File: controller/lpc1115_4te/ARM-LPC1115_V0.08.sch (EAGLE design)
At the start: 52 parts, among them IC2 MC34063AP, IC3 MCP1702-33, Q1 BC557B, Q3 BC640C, T1 BC547C

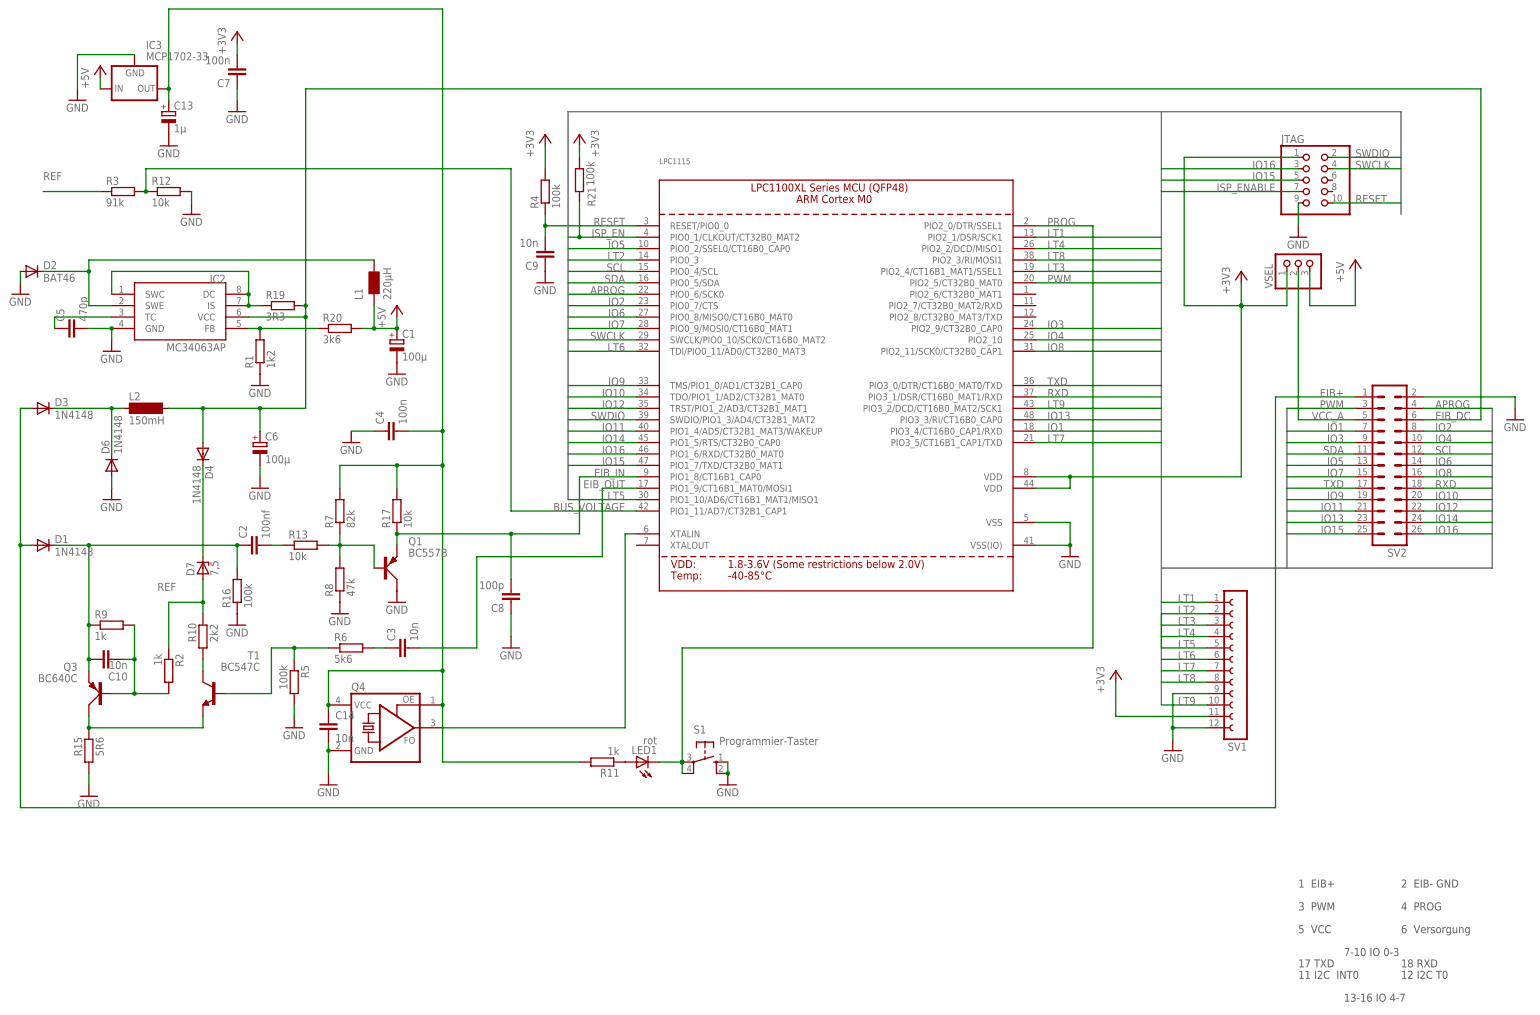
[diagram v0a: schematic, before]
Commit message: Improve layout
Changed routing to create better ground plane on bottom layer.
Add C11 to proviode better/more stable voltage supply to the CPU.
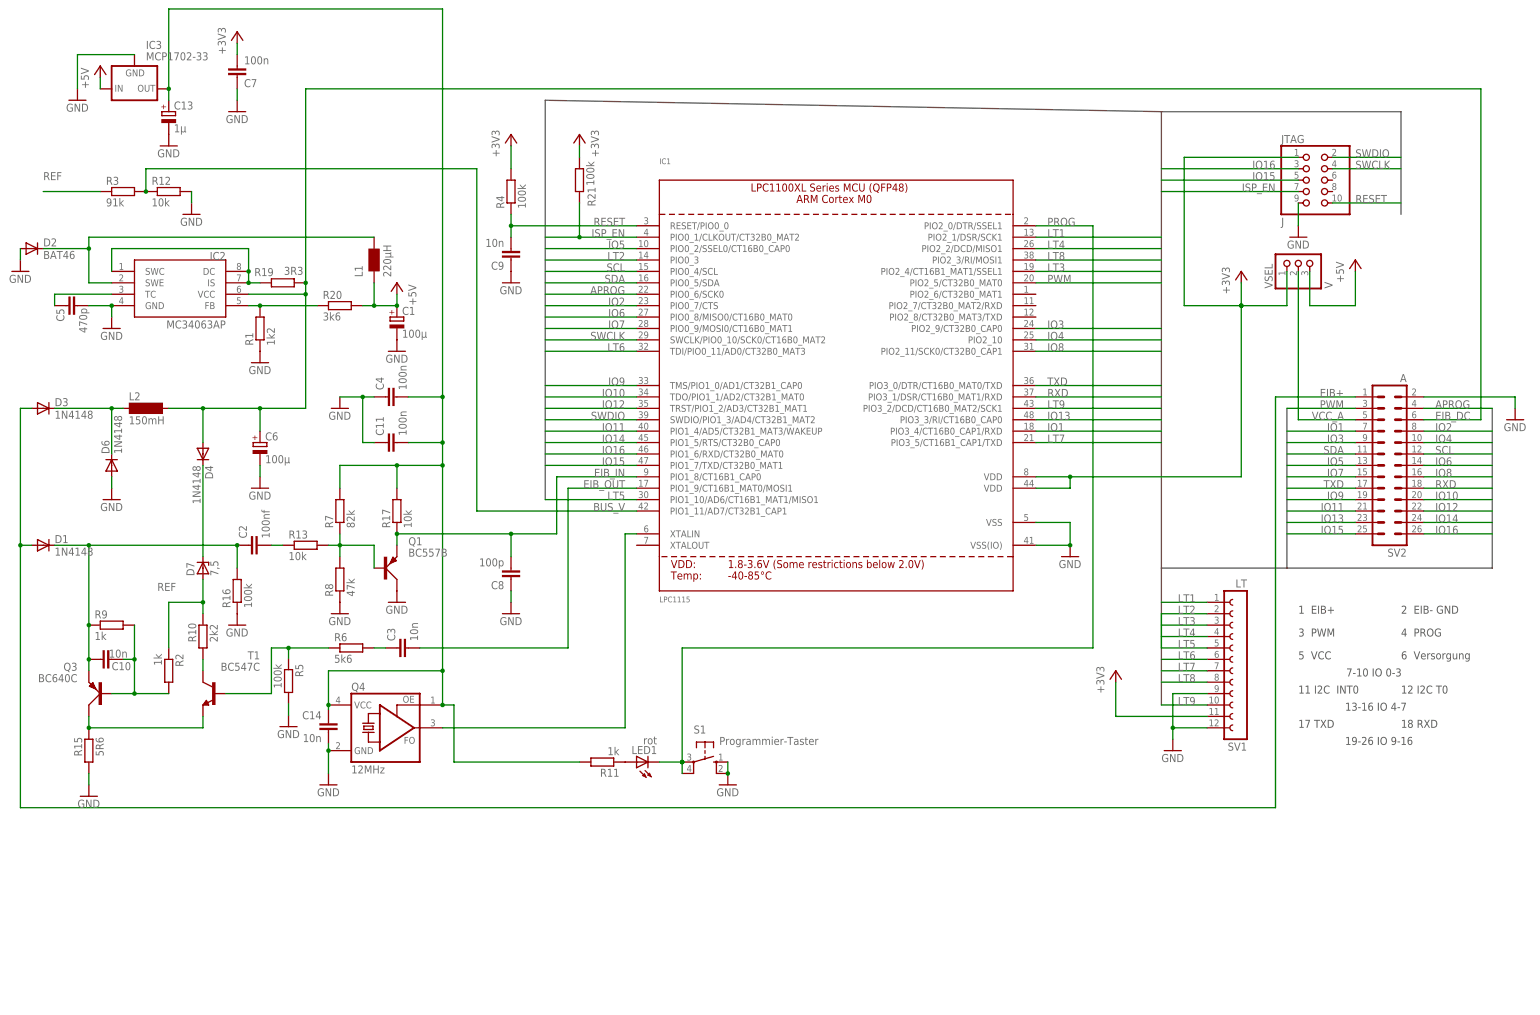
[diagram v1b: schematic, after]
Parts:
- added C11: 100n, rcl:C-EU050-024X044
- IC1: value (none) -> LPC1115
- JTAG: value (none) -> J
- Q4: value (none) -> 12MHz
- SV1: value (none) -> LT
- SV2: value (none) -> A
- VSEL: value (none) -> V
- renumbered LPC1115 to IC1
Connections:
- net BUS_VOLTAGE renamed BUS_V
- removed net ISP_ENABLE: JTAG.7
- net GND: now also C11.1
- net ISP_EN: now also JTAG.7
- net VCC_3V3: now also C11.2
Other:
- note added: "19-26 IO 9-16"
- moved on the sheet: C1, C4, C5, C8, C9, D2, IC2, L1, R1, R19, R20, R4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

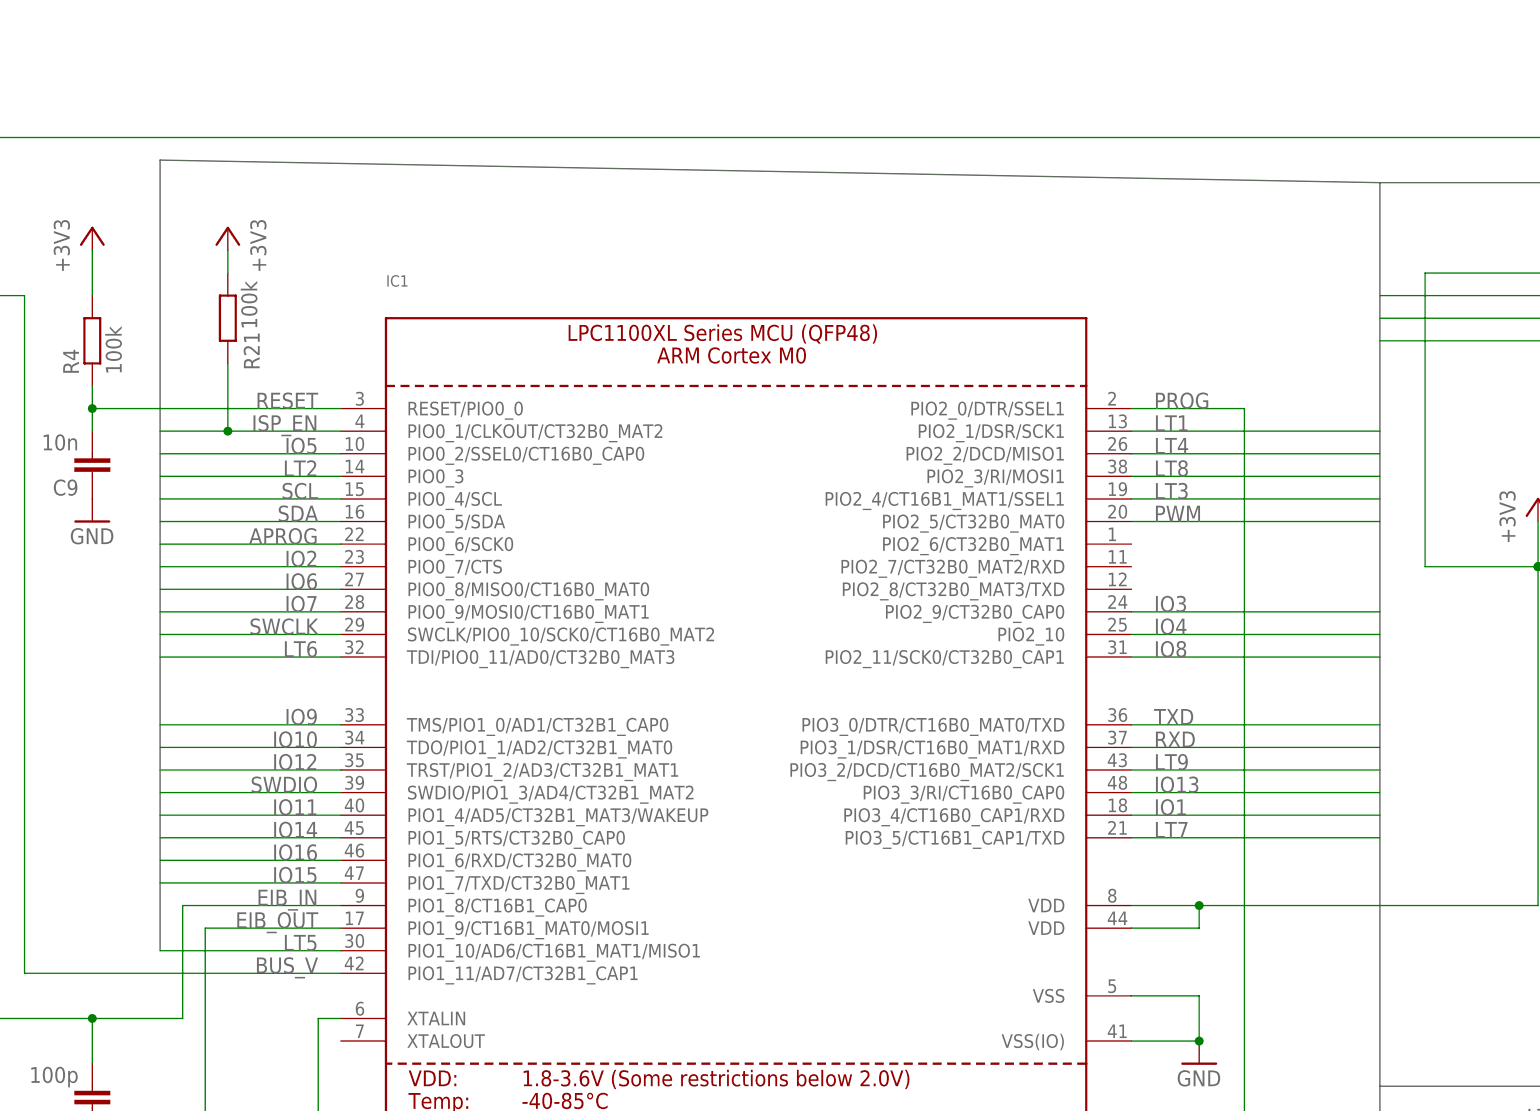
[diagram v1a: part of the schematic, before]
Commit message: Exchange PWM and LT9
To support a LPC11Uxx device and have the two pins required for the USB on
the LED/Taster pinhead the old PWM and LT9 have been swaped.
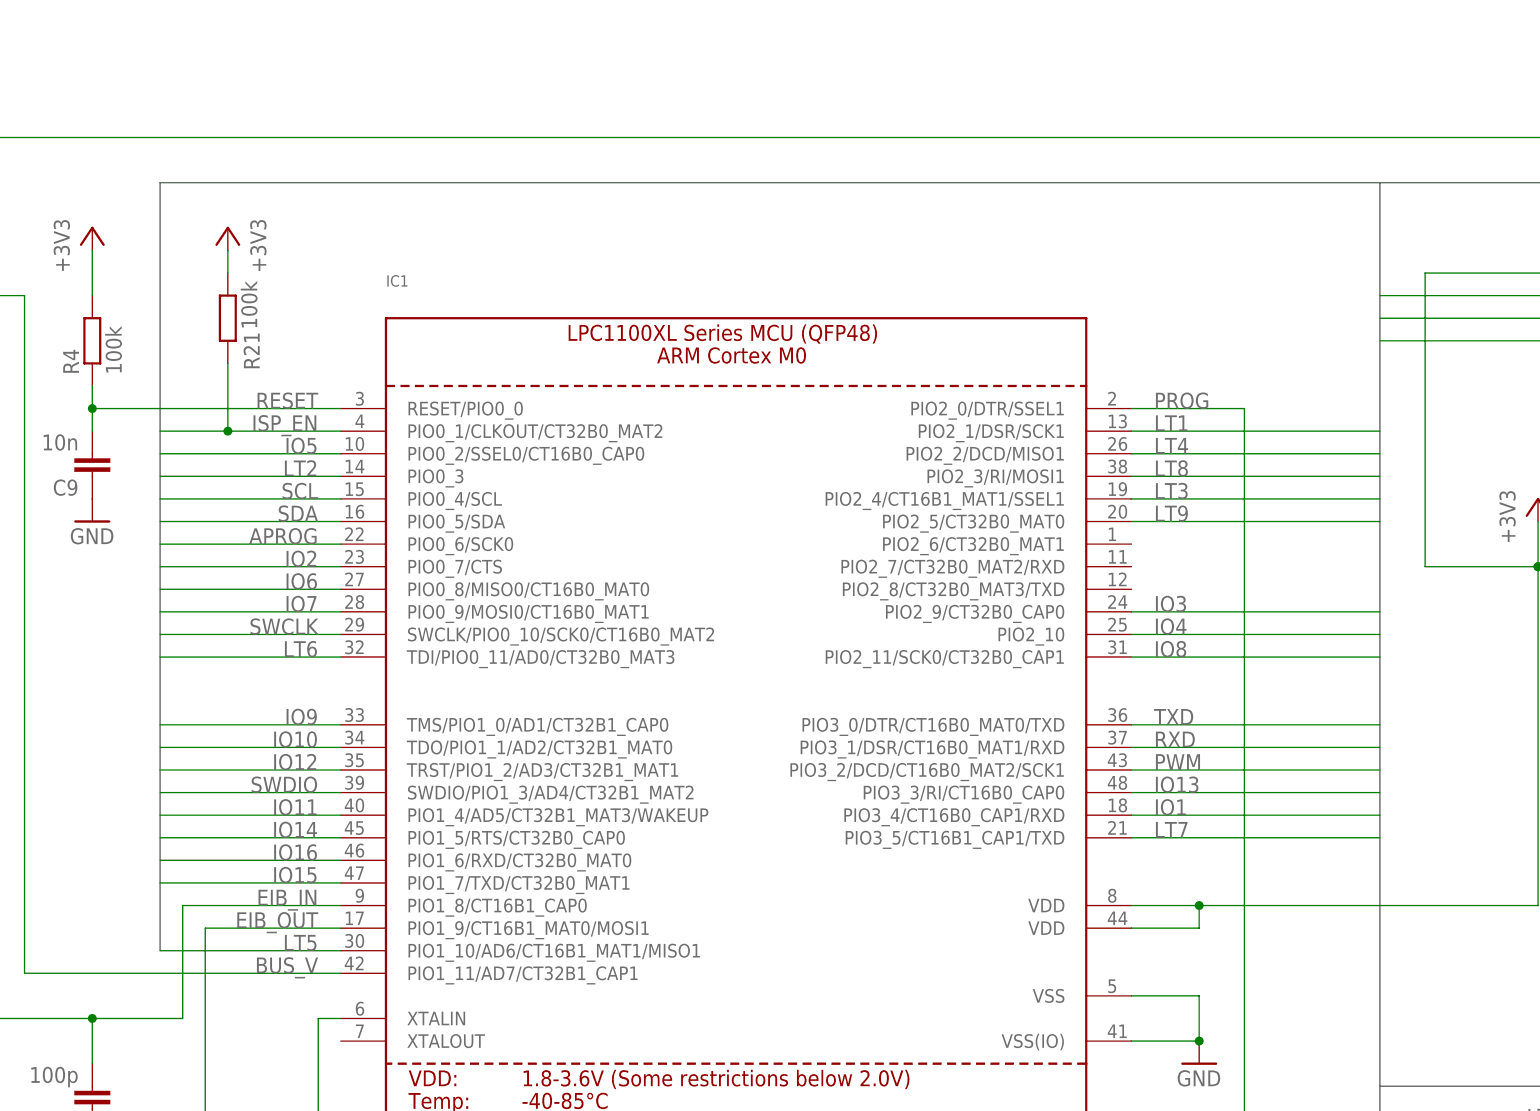
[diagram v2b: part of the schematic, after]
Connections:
- net LT9: now also IC1.PIO2_5/CT32B0_MAT0; no longer IC1.PIO3_2/DCD/CT16B0_MAT2/SCK1
- net PWM: now also IC1.PIO3_2/DCD/CT16B0_MAT2/SCK1; no longer IC1.PIO2_5/CT32B0_MAT0
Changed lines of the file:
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@@
 <?xml version="1.0" encoding="utf-8"?>
 <!DOCTYPE eagle SYSTEM "eagle.dtd">
-<eagle version="6.5.0">
+<eagle version="6.4">
 <drawing>
 <settings>
@@
 <wire x1="309.88" y1="45.72" x2="309.88" y2="81.28" width="0.762" layer="92"/>
 <wire x1="236.22" y1="45.72" x2="236.22" y2="147.32" width="0.762" layer="92"/>
-<wire x1="236.22" y1="147.32" x2="99.06" y2="149.86" width="0.762" layer="92"/>
-<wire x1="99.06" y1="149.86" x2="99.06" y2="60.96" width="0.762" layer="92"/>
+<wire x1="236.22" y1="147.32" x2="99.06" y2="147.32" width="0.762" layer="92"/>
+<wire x1="99.06" y1="147.32" x2="99.06" y2="60.96" width="0.762" layer="92"/>
 <wire x1="236.22" y1="45.72" x2="236.22" y2="15.24" width="0.762" layer="92"/>
 <wire x1="236.22" y1="147.32" x2="289.56" y2="147.32" width="0.762" layer="92"/>
@@
 <net name="PWM" class="0">
 <segment>
-<pinref part="IC1" gate="G$1" pin="PIO2_5/CT32B0_MAT0"/>
-<wire x1="236.22" y1="109.22" x2="208.28" y2="109.22" width="0.1524" layer="91"/>
-<label x="210.82" y="109.22" size="1.778" layer="95"/>
-</segment>
-<segment>
 <pinref part="SV2" gate="1" pin="3"/>
 <wire x1="279.4" y1="81.28" x2="264.16" y2="81.28" width="0.1524" layer="91"/>
 <label x="276.86" y="81.28" size="1.778" layer="95" rot="MR0"/>
+</segment>
+<segment>
+<pinref part="IC1" gate="G$1" pin="PIO3_2/DCD/CT16B0_MAT2/SCK1"/>
+<wire x1="236.22" y1="81.28" x2="208.28" y2="81.28" width="0.1524" layer="91"/>
+<label x="210.82" y="81.28" size="1.778" layer="95"/>
 </segment>
 </net>
@@
 <net name="LT9" class="0">
 <segment>
-<pinref part="IC1" gate="G$1" pin="PIO3_2/DCD/CT16B0_MAT2/SCK1"/>
-<wire x1="236.22" y1="81.28" x2="208.28" y2="81.28" width="0.1524" layer="91"/>
-<label x="210.82" y="81.28" size="1.778" layer="95"/>
-</segment>
-<segment>
 <pinref part="SV1" gate="G$1" pin="10"/>
 <wire x1="246.38" y1="15.24" x2="236.22" y2="15.24" width="0.1524" layer="91"/>
 <label x="243.84" y="15.24" size="1.778" layer="95" rot="MR0"/>
 </segment>
-</net>
+<segment>
+<pinref part="IC1" gate="G$1" pin="PIO2_5/CT32B0_MAT0"/>
+<wire x1="236.22" y1="109.22" x2="208.28" y2="109.22" width="0.1524" layer="91"/>
+<label x="210.82" y="109.22" size="1.778" layer="95"/>
+</segment>
+</net>
